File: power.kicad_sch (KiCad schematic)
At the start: 16 parts, among them IC3 TPS62441RQRR, U12 BQ24075RGT

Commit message: did power and usb
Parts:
- removed C88, C90: 4.7uF, Capacitor_SMD:C_0402_1005Metric, symbol Device:C
- added BT1: Battery_Cell, symbol Device:Battery_Cell
- added C10, C9: 10uF, symbol Device:C
- added C11: 100nF, symbol Device:C
- added C7, C8: 10pF, symbol Device:C
- added C93, C94, C95: 4.7uF, Capacitor_SMD:C_0402_1005Metric, symbol Device:C
- added L1, L2: 0.47 μH, symbol Device:L
- added R2: 88.7k, symbol Device:R
- added R3: 19.6k, symbol Device:R
- added R4: 80.6k, symbol Device:R
- added R5: 40.2k, symbol Device:R
- added R6: 100k, symbol Device:R
- added TP1: 1.8V PG, symbol Connector:TestPoint
- added TP2: 3.3V PG, symbol Connector:TestPoint
- R1: value R -> 100k
- R28: value 3.9k -> 1.7k
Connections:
- net VSW is gone; now on net +5V: U12.6 (EN1)
- net +1V8: now also C8.1, L1.2, R4.2; no longer IC3.12 (SW2)
- net +3V3: now also C7.1, L2.1, R2.2; no longer IC3.6 (SW1)
- net +5V: now also C10.1, C11.1, C9.1, C94.2
- net FB1: now also C7.2, R2.1, R3.2
- net FB2: now also C8.2, R4.1, R5.2
- net GND: now also IC3.14 (COMP_/FSET), BT1.2 (-), C10.2, C11.2, C9.2, C93.1, C94.1, C95.1, R3.1, R5.1; no longer R1.1, U12.5 (EN2)
- net REG-OUT: now also R1.2, C95.2, R6.2
- net VBAT: now also BT1.1 (+), C93.2
- net PG2: now reaches IC3.13 (PG2)
- net PG2: now also R1.1, TP1.1
- net PG1: now reaches IC3.4 (PG1)
- net PG1: now also R6.1, TP2.1
- new net: IC3.6 (SW1), L2.2
- new net: IC3.12 (SW2), L1.1
- new net EN2: U12.5 (EN2)
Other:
- note added: "RISET = 890A*OHM / ICHG ICHG <=1.5A ILIM does no matter, becouse en1 and en2 set it to usb500mA"
- moved on the sheet: C92, R28, R30, R32, R34, U12

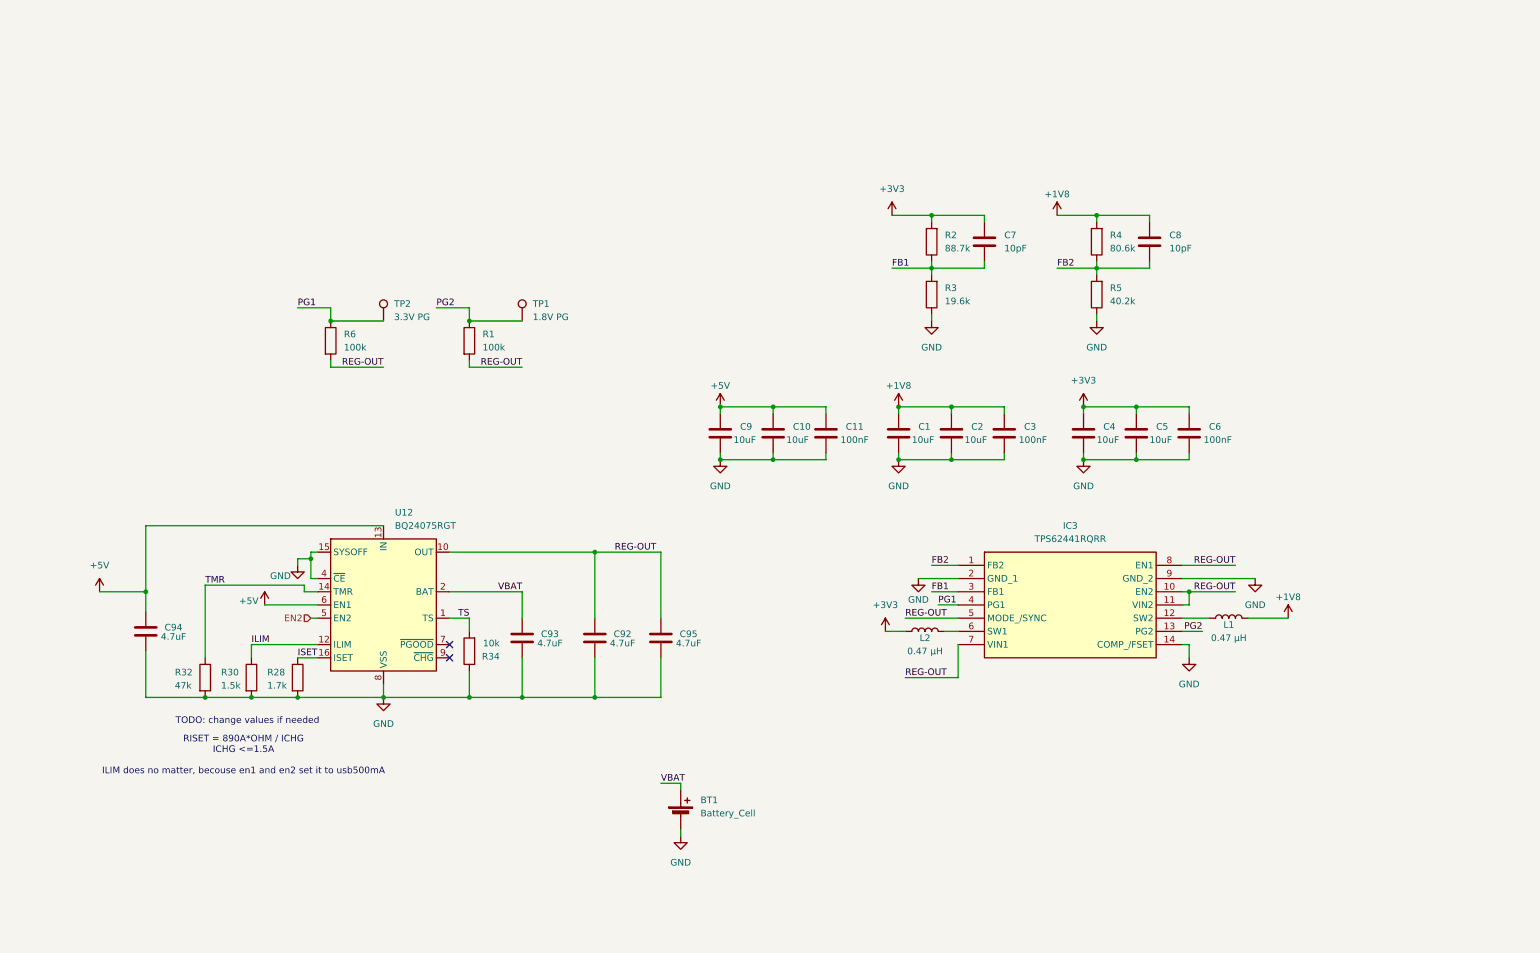
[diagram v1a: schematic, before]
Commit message: changed the switch converter to a LDOs
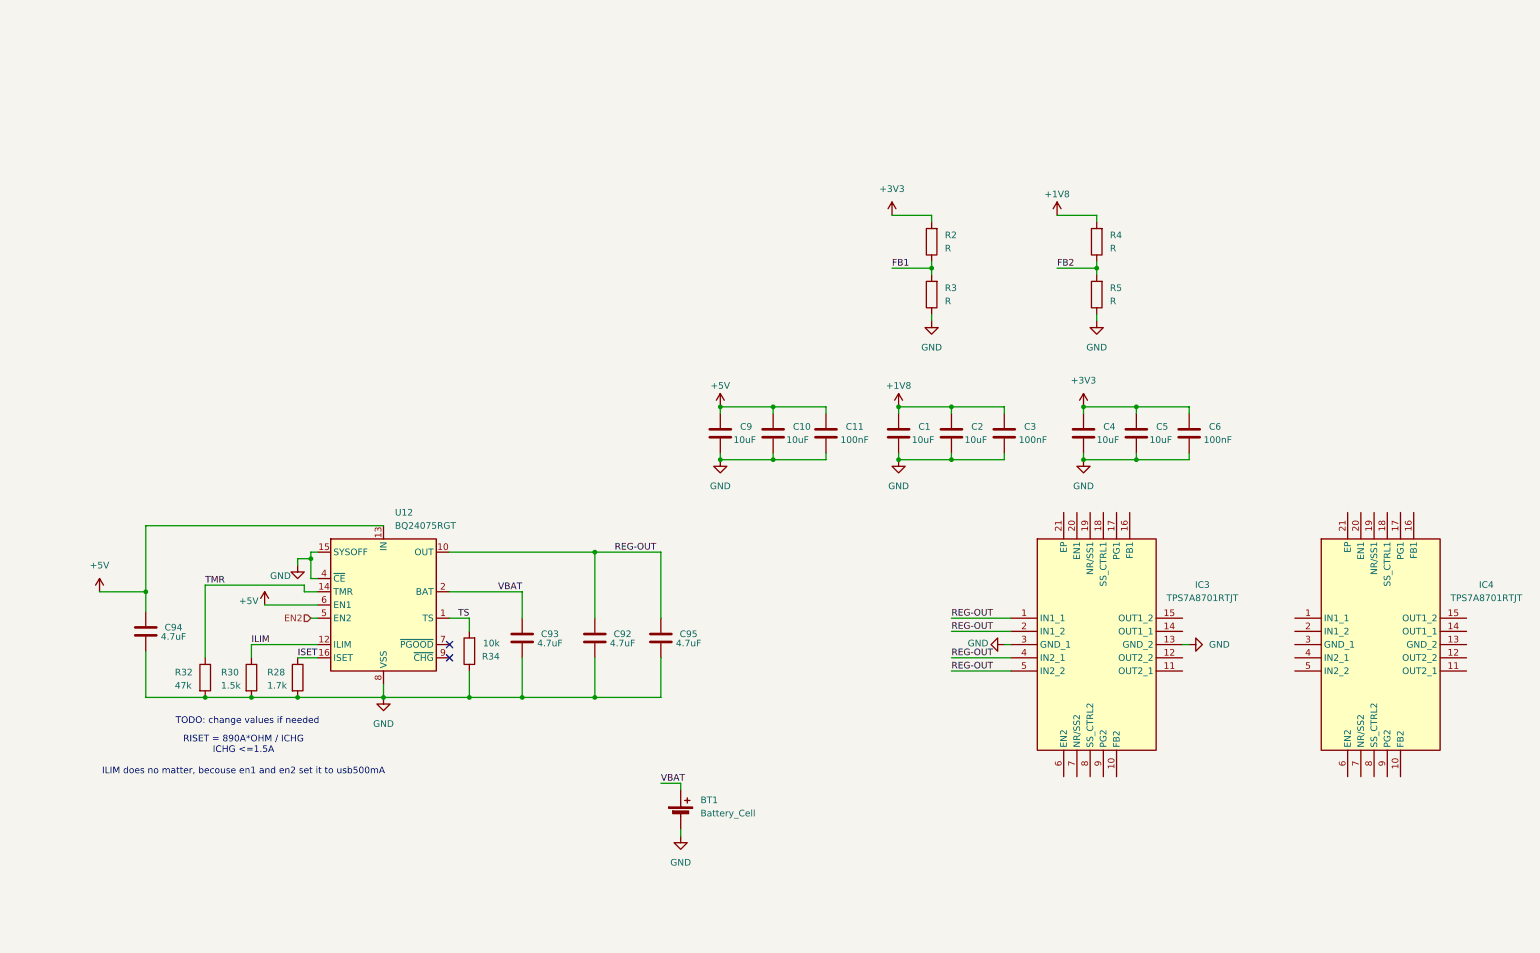
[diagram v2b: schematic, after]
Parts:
- removed C7, C8: 10pF, symbol Device:C
- removed IC3: TPS62441RQRR, TPS62441RQRR, symbol TPS62441RQRR:TPS62441RQRR
- removed L1, L2: 0.47 μH, symbol Device:L
- removed R1, R6: 100k, symbol Device:R
- removed TP1: 1.8V PG, symbol Connector:TestPoint
- removed TP2: 3.3V PG, symbol Connector:TestPoint
- added IC3, IC4: TPS7A8701RTJT, QFN50P400X400X80-21N-D, symbol TPS7A8701RTJT:TPS7A8701RTJT
- R2: value 88.7k -> R
- R3: value 19.6k -> R
- R4: value 80.6k -> R
- R5: value 40.2k -> R
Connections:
- net GND: now also IC3.13 (GND_2), IC3.3 (GND_1)
- net REG-OUT: now also IC3.1 (IN1_1), IC3.2 (IN1_2), IC3.4 (IN2_1), IC3.5 (IN2_2)

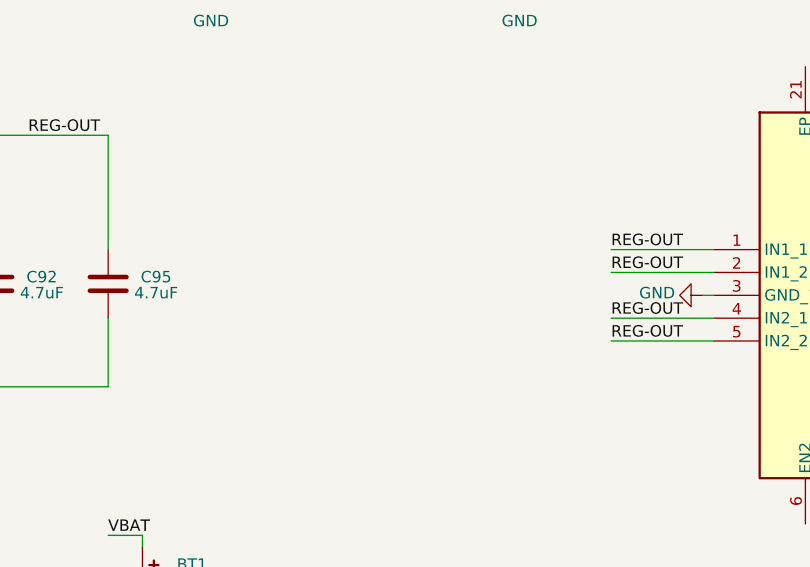
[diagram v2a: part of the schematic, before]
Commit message: added the sd card slot
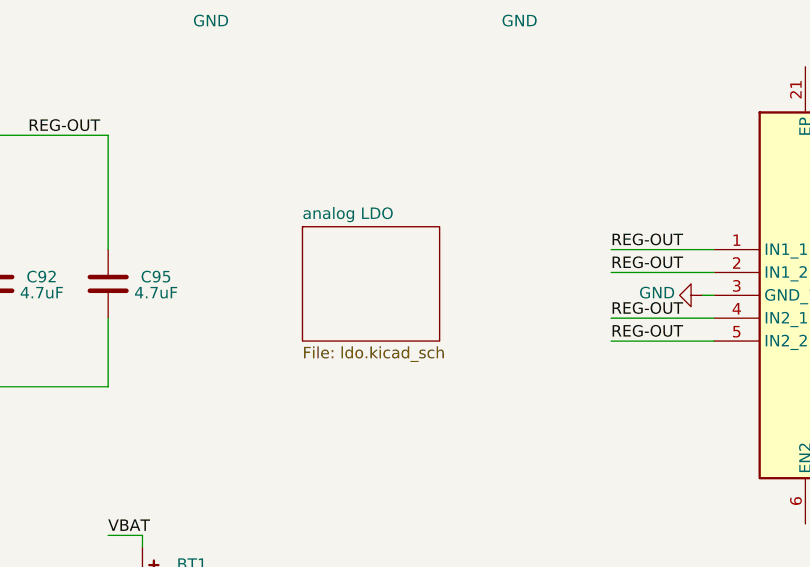
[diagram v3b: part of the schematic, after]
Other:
- added sheet analog LDO (ldo.kicad_sch)
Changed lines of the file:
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@@
+		)
+	)
+	(sheet
+		(at 167.64 130.81)
+		(size 15.24 12.7)
+		(exclude_from_sim no)
+		(in_bom yes)
+		(on_board yes)
+		(dnp no)
+		(fields_autoplaced yes)
+		(stroke
+			(width 0.1524)
+			(type solid)
+		)
+		(fill
+			(color 0 0 0 0.0000)
+		)
+		(property "Sheetname" "analog LDO"
+			(at 167.64 130.0984 0)
+			(effects
+				(font
+					(size 1.27 1.27)
+				)
+				(justify left bottom)
+			)
+		)
+		(property "Sheetfile" "ldo.kicad_sch"
+			(at 167.64 144.0946 0)
+			(effects
+				(font
+					(size 1.27 1.27)
+				)
+				(justify left top)
+			)
+		)
+		(instances
+			(project "meko-pcb"
+				(path "/bdd43acd-23c1-472b-909a-8e24eb60d56d/8a6dc5b3-4f2f-4276-a496-11a08be250c4"
+					(page "5")
+				)
+			)
 		)
 	)

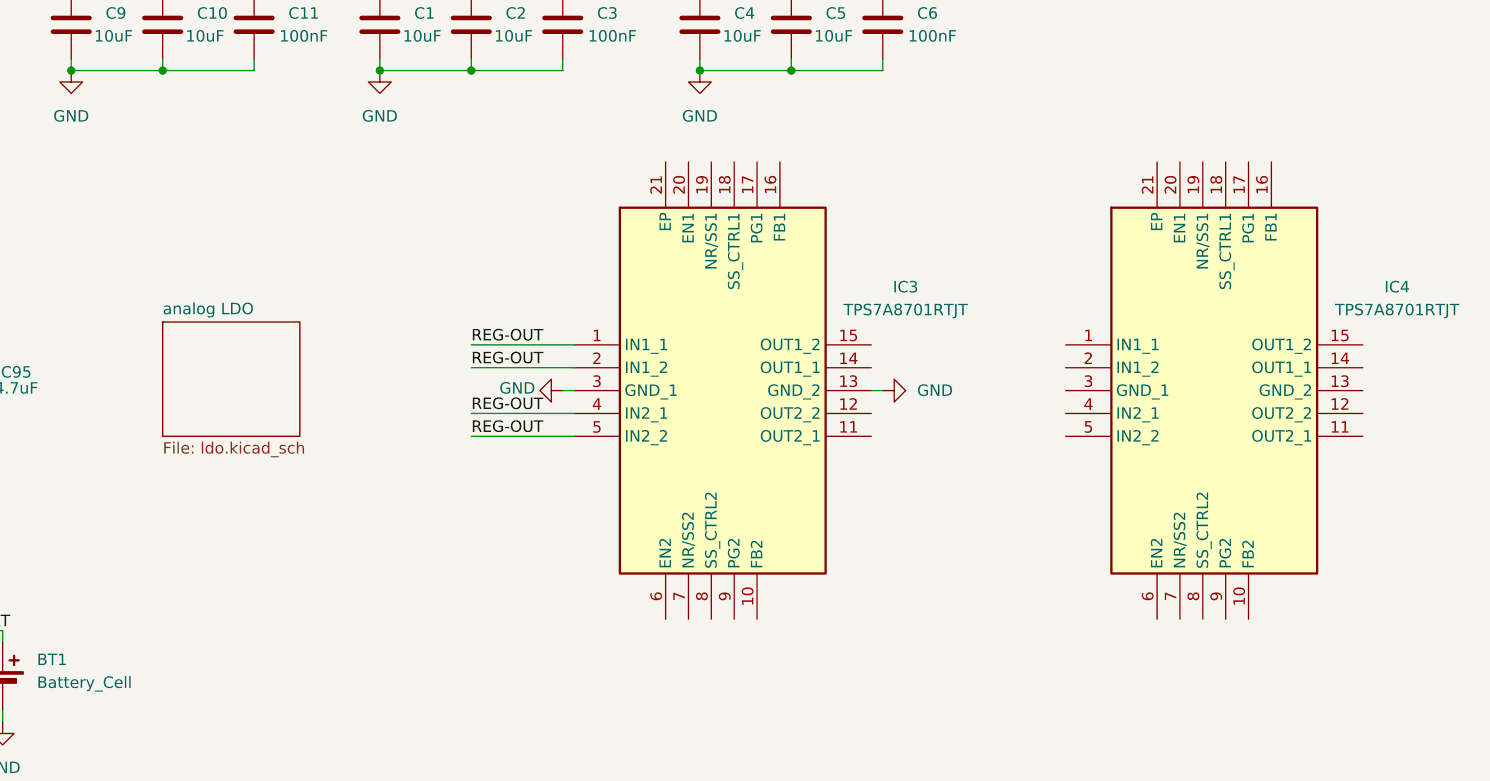
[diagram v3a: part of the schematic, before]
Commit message: removed old regulator, added new ones
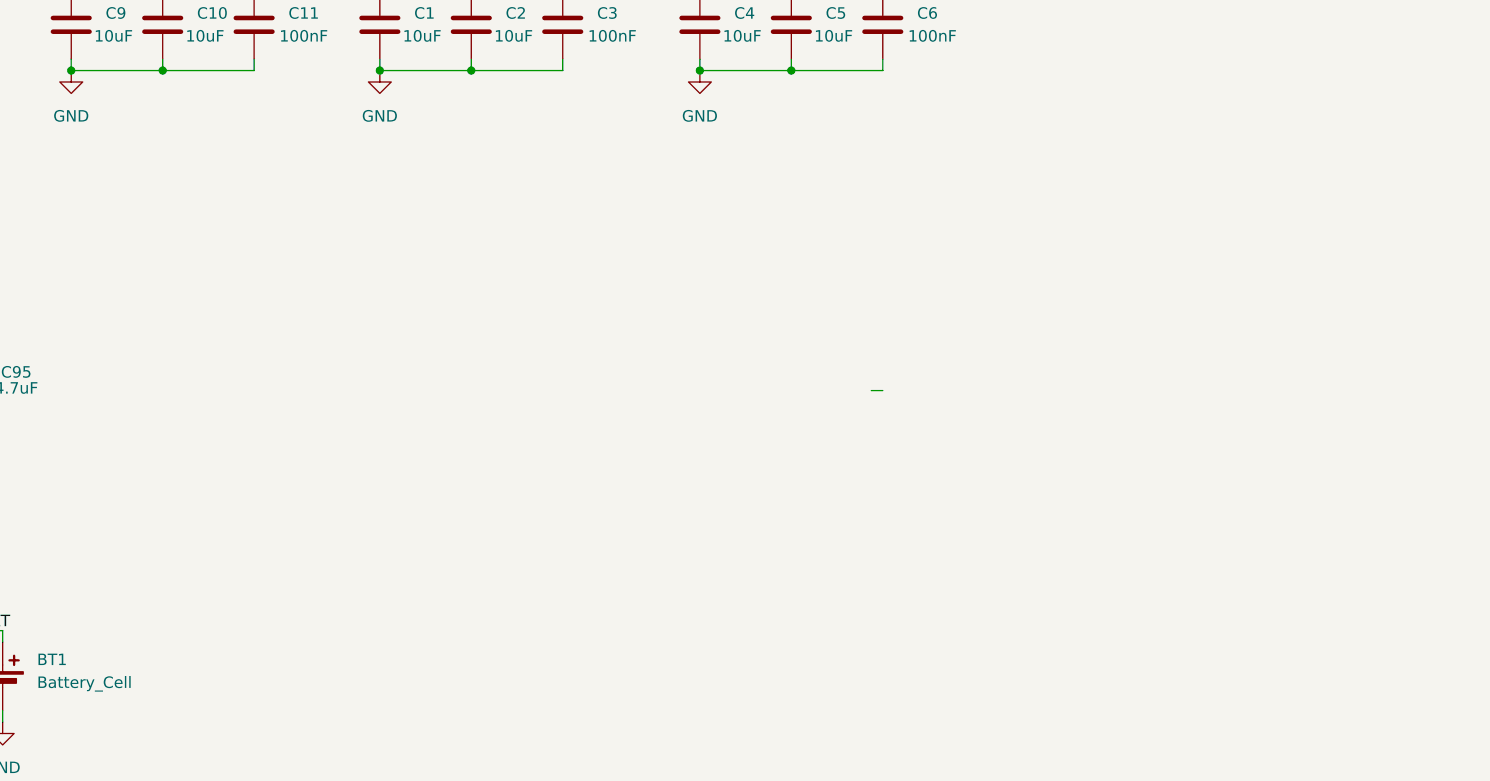
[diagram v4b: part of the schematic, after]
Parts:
- removed IC3, IC4: TPS7A8701RTJT, QFN50P400X400X80-21N-D, symbol TPS7A8701RTJT:TPS7A8701RTJT
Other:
- removed sheet analog LDO
